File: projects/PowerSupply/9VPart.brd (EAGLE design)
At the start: 50 x 50 mm, 26 parts, among them IC1 LM2596T, IC2 LM2596T, X1 IN, X2 OUT

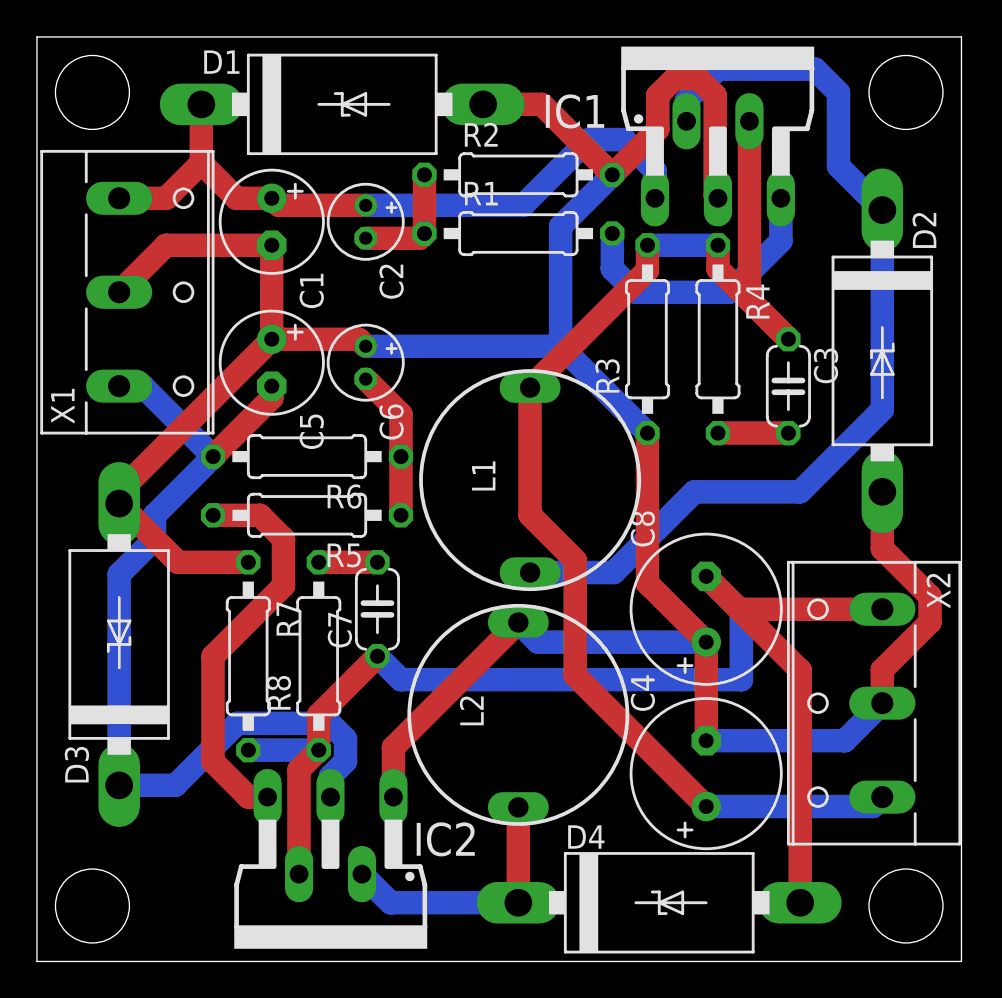
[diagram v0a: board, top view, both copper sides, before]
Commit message: feat: 9 volt part modified
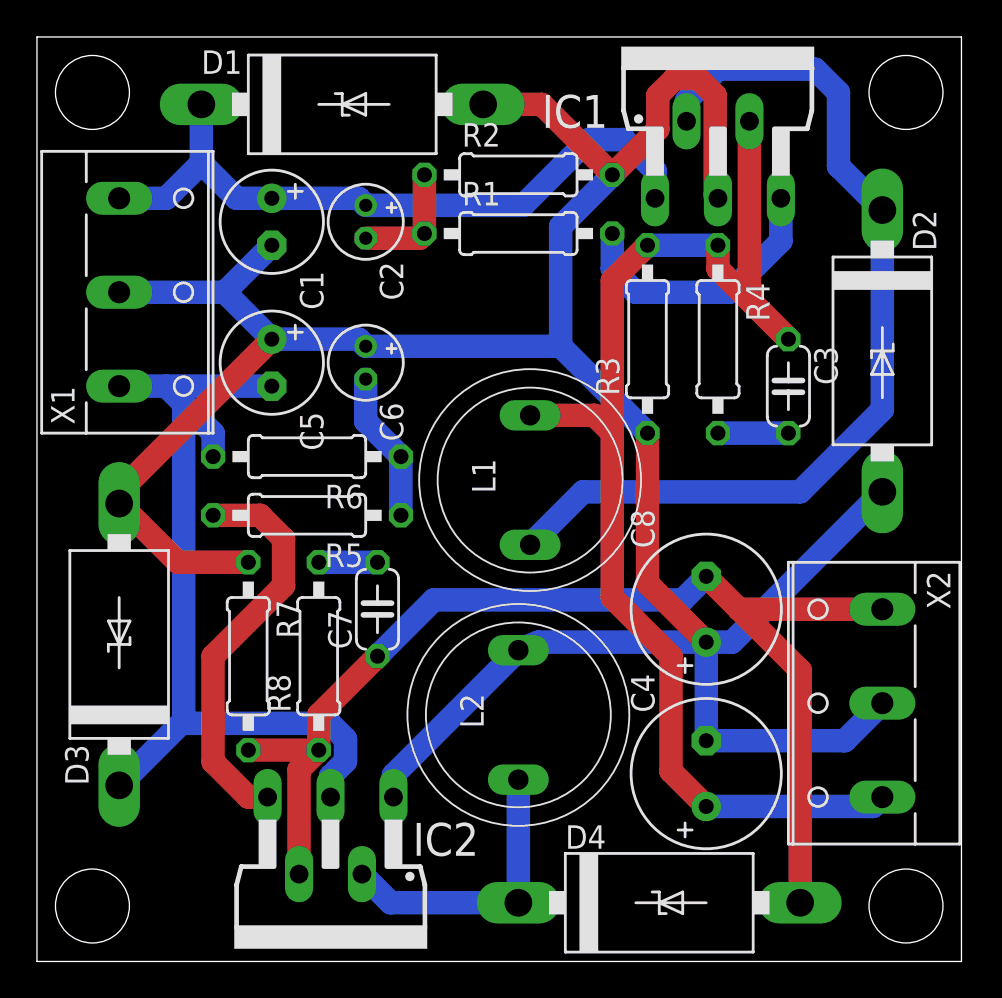
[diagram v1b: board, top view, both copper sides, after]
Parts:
- C8: value 330µF -> 470µF
- L1: device inductor-neosid:SD12-680 -> bb84:IND-120
- L2: value 47µH -> 33µH; device inductor-neosid:SD12-680 -> bb84:IND-120
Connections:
- net +9V: now also L1.P$2; no longer L1.2
- net GND: now also L2.P$2; no longer L2.2
- net N$2: now also L2.P$1; no longer L2.1
- net N$3: now also L1.P$1; no longer L1.1
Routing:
- net -9V: track 71.4 -> 64.4 mm
- net GND: track 155.9 -> 151.9 mm
- net N$2: track 14.3 -> 15.8 mm
- net -20V: track 49.1 -> 47.8 mm
- net +9V: track 69.8 -> 71.0 mm
- net N$3: track 51.4 -> 50.8 mm

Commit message: feat: 5 volt part rerouted
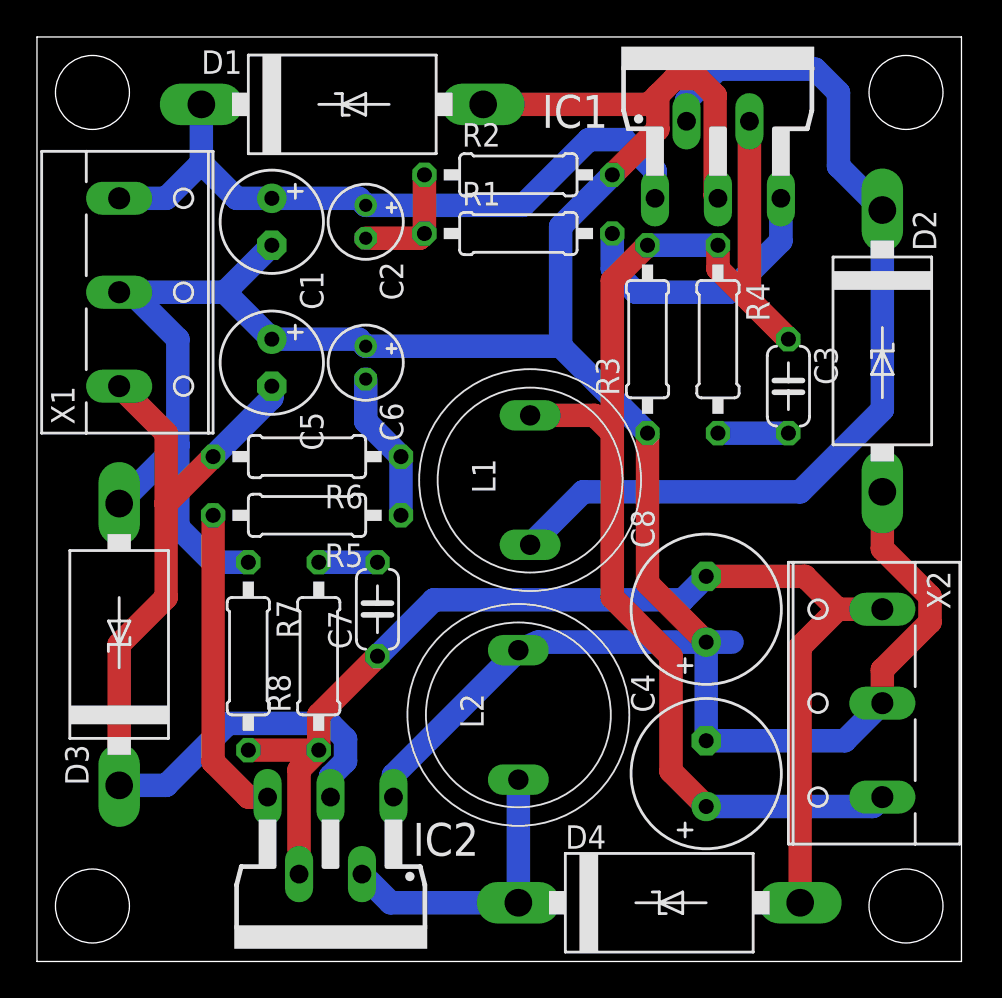
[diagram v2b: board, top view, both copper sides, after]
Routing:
- net GND: track 151.9 -> 158.0 mm
- net N$7: track 21.7 -> 17.1 mm
- net -20V: track 47.8 -> 49.9 mm
- net -9V: track 64.4 -> 63.9 mm
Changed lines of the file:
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@@
 <contactref element="X2" pad="2"/>
 <contactref element="X1" pad="2"/>
-<wire x1="12.7" y1="33.655" x2="4.445" y2="25.4" width="1.27" layer="1"/>
-<wire x1="4.445" y1="25.4" x2="4.445" y2="24.765" width="1.27" layer="1"/>
-<wire x1="4.445" y1="24.765" x2="7.62" y2="21.59" width="1.27" layer="1"/>
-<wire x1="7.62" y1="21.59" x2="11.43" y2="21.59" width="1.27" layer="1"/>
 <wire x1="36.195" y1="17.272" x2="33.02" y2="20.447" width="1.27" layer="1"/>
 <wire x1="33.02" y1="20.447" x2="33.02" y2="28.575" width="1.27" layer="1"/>
@@
 <wire x1="36.83" y1="41.275" x2="36.6776" y2="41.4274" width="1.27" layer="1"/>
 <wire x1="36.6776" y1="41.4274" x2="36.6776" y2="46.8443875" width="1.27" layer="1"/>
-<wire x1="24.13" y1="46.355" x2="27.305" y2="46.355" width="1.27" layer="1"/>
-<wire x1="27.305" y1="46.355" x2="31.115" y2="42.545" width="1.27" layer="1"/>
 <wire x1="36.195" y1="11.938" x2="43.688" y2="11.938" width="1.27" layer="16"/>
 <wire x1="43.688" y1="11.938" x2="45.72" y2="13.97" width="1.27" layer="16"/>
@@
 <wire x1="28.321" y1="39.751" x2="28.321" y2="33.274" width="1.27" layer="16"/>
 <wire x1="36.195" y1="17.272" x2="37.592" y2="17.272" width="1.27" layer="16"/>
-<wire x1="37.592" y1="17.272" x2="45.72" y2="25.4" width="1.27" layer="16"/>
 <wire x1="36.195" y1="17.272" x2="36.195" y2="11.938" width="1.27" layer="16"/>
 <wire x1="4.445" y1="36.195" x2="10.16" y2="36.195" width="1.27" layer="16"/>
@@
 <wire x1="19.2786" y1="8.89" x2="19.2786" y2="10.0786" width="1.27" layer="16"/>
 <wire x1="19.2786" y1="10.0786" x2="26.035" y2="16.835" width="1.27" layer="16"/>
+<wire x1="11.43" y1="21.59" x2="9.525" y2="21.59" width="1.27" layer="16"/>
+<wire x1="9.525" y1="21.59" x2="7.62" y2="23.495" width="1.27" layer="16"/>
+<wire x1="7.62" y1="23.495" x2="7.62" y2="27.94" width="1.27" layer="16"/>
+<wire x1="7.62" y1="27.94" x2="7.62" y2="33.655" width="1.27" layer="16"/>
+<wire x1="7.62" y1="33.655" x2="5.08" y2="36.195" width="1.27" layer="16"/>
+<wire x1="5.08" y1="36.195" x2="4.445" y2="36.195" width="1.27" layer="16"/>
+<wire x1="4.445" y1="24.765" x2="7.62" y2="27.94" width="1.27" layer="16"/>
+<wire x1="33.0894125" y1="46.355" x2="33.5788" y2="46.8443875" width="1.27" layer="1"/>
+<wire x1="24.13" y1="46.355" x2="33.0894125" y2="46.355" width="1.27" layer="1"/>
+<wire x1="48.2981" y1="19.74701875" x2="48.2981" y2="18.35298125" width="1.27" layer="1"/>
+<wire x1="45.72" y1="25.4" x2="45.72" y2="22.32511875" width="1.27" layer="1"/>
+<wire x1="45.72" y1="15.77488125" x2="45.72" y2="13.97" width="1.27" layer="1"/>
+<wire x1="45.72" y1="22.32511875" x2="48.2981" y2="19.74701875" width="1.27" layer="1"/>
+<wire x1="48.2981" y1="18.35298125" x2="45.72" y2="15.77488125" width="1.27" layer="1"/>
 </signal>
 <signal name="N$3">
@@
 <contactref element="R5" pad="2"/>
 <contactref element="IC2" pad="5"/>
-<wire x1="9.525" y1="24.13" x2="12.065" y2="24.13" width="1.27" layer="1"/>
-<wire x1="12.065" y1="24.13" x2="13.335" y2="22.86" width="1.27" layer="1"/>
-<wire x1="13.335" y1="22.86" x2="13.335" y2="20.32" width="1.27" layer="1"/>
-<wire x1="13.335" y1="20.32" x2="9.525" y2="16.51" width="1.27" layer="1"/>
-<wire x1="9.525" y1="16.51" x2="9.525" y2="10.795" width="1.27" layer="1"/>
-<wire x1="9.525" y1="10.795" x2="11.43" y2="8.89" width="1.27" layer="1"/>
+<wire x1="11.43" y1="8.89" x2="9.525" y2="10.795" width="1.27" layer="1"/>
 <wire x1="11.43" y1="8.89" x2="12.4714" y2="8.89" width="1.27" layer="1"/>
+<wire x1="9.525" y1="10.795" x2="9.525" y2="24.13" width="1.27" layer="1"/>
 </signal>
 <signal name="N$8">
@@
 <wire x1="15.24" y1="11.43" x2="15.24" y2="13.335" width="1.27" layer="1"/>
 <wire x1="15.24" y1="13.335" x2="18.415" y2="16.51" width="1.27" layer="1"/>
-<wire x1="41.275" y1="15.748" x2="41.275" y2="3.175" width="1.27" layer="1"/>
-<wire x1="45.72" y1="19.05" x2="37.973" y2="19.05" width="1.27" layer="1"/>
-<wire x1="36.195" y1="20.828" x2="37.973" y2="19.05" width="1.27" layer="1"/>
-<wire x1="37.973" y1="19.05" x2="41.275" y2="15.748" width="1.27" layer="1"/>
+<wire x1="41.275" y1="17.018" x2="41.275" y2="3.175" width="1.27" layer="1"/>
 <wire x1="18.415" y1="16.51" x2="21.463" y2="19.558" width="1.27" layer="16"/>
 <wire x1="34.925" y1="19.558" x2="21.463" y2="19.558" width="1.27" layer="16"/>
 <wire x1="34.925" y1="19.558" x2="36.195" y2="20.828" width="1.27" layer="16"/>
 <wire x1="11.43" y1="11.43" x2="15.24" y2="11.43" width="1.27" layer="1"/>
+<wire x1="45.72" y1="19.05" x2="43.307" y2="19.05" width="1.27" layer="1"/>
+<wire x1="43.307" y1="19.05" x2="41.275" y2="17.018" width="1.27" layer="1"/>
+<wire x1="36.195" y1="20.828" x2="41.529" y2="20.828" width="1.27" layer="1"/>
+<wire x1="41.529" y1="20.828" x2="43.307" y2="19.05" width="1.27" layer="1"/>
 </signal>
 <signal name="+20V">
@@
 <wire x1="15.875" y1="8.89" x2="15.875" y2="10.0175" width="1.27" layer="16"/>
 <wire x1="15.875" y1="10.0175" x2="16.6878" y2="10.8303" width="1.27" layer="16"/>
-<wire x1="4.445" y1="31.115" x2="6.985" y2="31.115" width="1.27" layer="16"/>
-<wire x1="6.985" y1="31.115" x2="12.7" y2="31.115" width="1.27" layer="16"/>
-<wire x1="6.985" y1="31.115" x2="7.9375" y2="30.1625" width="1.27" layer="16"/>
-<wire x1="7.9375" y1="30.1625" x2="9.525" y2="28.575" width="1.27" layer="16"/>
-<wire x1="9.525" y1="28.575" x2="9.525" y2="27.305" width="1.27" layer="16"/>
-<wire x1="7.9375" y1="30.1625" x2="7.9375" y2="13.0175" width="1.27" layer="16"/>
-<wire x1="7.9375" y1="13.0175" x2="4.445" y2="9.525" width="1.27" layer="16"/>
-<wire x1="8.0772" y1="12.8778" x2="7.9375" y2="13.0175" width="1.27" layer="16"/>
-<wire x1="15.8397" y1="12.8778" x2="8.0772" y2="12.8778" width="1.27" layer="16"/>
+<wire x1="12.7" y1="30.48" x2="12.7" y2="31.115" width="1.27" layer="16"/>
+<wire x1="12.7" y1="30.48" x2="9.525" y2="27.305" width="1.27" layer="16"/>
+<wire x1="15.8397" y1="12.8778" x2="10.3378" y2="12.8778" width="1.27" layer="16"/>
+<wire x1="10.3378" y1="12.8778" x2="6.985" y2="9.525" width="1.27" layer="16"/>
+<wire x1="6.985" y1="9.525" x2="4.445" y2="9.525" width="1.27" layer="16"/>
+<wire x1="4.445" y1="31.115" x2="6.985" y2="28.575" width="1.27" layer="1"/>
+<wire x1="6.985" y1="28.575" x2="6.985" y2="24.765" width="1.27" layer="1"/>
+<wire x1="6.985" y1="24.765" x2="6.985" y2="19.685" width="1.27" layer="1"/>
+<wire x1="6.985" y1="19.685" x2="4.445" y2="17.145" width="1.27" layer="1"/>
+<wire x1="4.445" y1="17.145" x2="4.445" y2="9.525" width="1.27" layer="1"/>
+<wire x1="9.525" y1="27.305" x2="6.985" y2="24.765" width="1.27" layer="1"/>
 </signal>
 </signals>
